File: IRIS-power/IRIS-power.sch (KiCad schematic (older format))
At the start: 66 parts, among them J2 Powerpole, J3 PJ-047AH

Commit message: Added new 5V rail, adjusted passives, added fuel gauge
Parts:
- removed C11: 1nF, Capacitor_SMD:C_0603_1608Metric, symbol Device:C
- removed C12, C14, C23: 10uF, Capacitor_SMD:C_1206_3216Metric, symbol Device:C
- removed C15: 10pF, Capacitor_SMD:C_0603_1608Metric, symbol Device:C
- removed C16: 1.2nF, Capacitor_SMD:C_0603_1608Metric, symbol Device:C
- removed C17, C20: 100nF, Capacitor_SMD:C_0603_1608Metric, symbol Device:C
- removed C18: 68nF, Capacitor_SMD:C_0603_1608Metric, symbol Device:C
- removed C21, C22: 22uF, Capacitor_SMD:C_1206_3216Metric, symbol Device:C
- removed C6: 150uF, Capacitor_SMD:C_1210_3225Metric, symbol Device:C
- removed C9: 220nF, Capacitor_SMD:C_0603_1608Metric, symbol Device:C
- removed D1: FSV1045V, STARpower:TO-227, symbol Device:D_Schottky
- removed L1: 1.5uH, STARpower:744314150, symbol Device:L
- removed L2: 3.3uH, STARpower:744316330, symbol Device:L
- removed L3: 10uH, STARpower:7443251000, symbol Device:L
- removed R1: 7.5k, Resistor_SMD:R_0603_1608Metric, symbol Device:R
- removed R11: 51.1R, Resistor_SMD:R_0603_1608Metric, symbol Device:R
- removed R12: 6.04k, Resistor_SMD:R_0603_1608Metric, symbol Device:R
- removed R15: 2.26k, Resistor_SMD:R_0603_1608Metric, symbol Device:R
- removed R17: 54.9k, Resistor_SMD:R_0603_1608Metric, symbol Device:R
- removed R18: 10k, Resistor_SMD:R_0603_1608Metric, symbol Device:R
- removed R2: 2.49k, Resistor_SMD:R_0603_1608Metric, symbol Device:R
- removed R3: 3.3k, Resistor_SMD:R_0603_1608Metric, symbol Device:R
- removed R6: 3320k, Resistor_SMD:R_0603_1608Metric, symbol Device:R
- removed R7: 1910k, Resistor_SMD:R_0603_1608Metric, symbol Device:R
- removed TP5, TP7: TestPoint, TestPoint:TestPoint_Loop_D2.60mm_Drill1.6mm_Beaded, symbol Connector:TestPoint
- removed U?: TPS565201, Package_TO_SOT_SMD:TSOT-23-6, symbol star-common-lib:TPS565201
- added C? (x3): 47uF, symbol Device:C
- added C? (x2): 10uF, symbol Device:C
- added C?: 68nF, symbol Device:C
- added C?: 1.2nF, symbol Device:C
- added C?: 0.47uF, symbol Device:C
- added C? (x2): 0.1uF, symbol Device:C
- added D?: D_Schottky, Diode_SMD:D_SMA_Handsoldering, symbol Device:D_Schottky
- added F?: Polyfuse, symbol Device:Polyfuse
- added JP? (x2): Jumper_3_Bridged12, symbol Jumper:Jumper_3_Bridged12
- added L?: 8.2uH, symbol Device:L
- added L?: 1.5uH, symbol Device:L
- added NT? (x4): Net-Tie_2, symbol Device:Net-Tie_2
- added Q?: 2N7002, Package_TO_SOT_SMD:SOT-23, symbol Transistor_FET:2N7002
- added Q?: IRLML6402, Package_TO_SOT_SMD:SOT-23, symbol Transistor_FET:IRLML6402
- added R? (x4): 10k, symbol Device:R
- added R? (x2): 2.49k, symbol Device:R
- added R? (x2): 3k, symbol Device:R
- added R?: 3570k, symbol Device:R
- added R?: 1150k, symbol Device:R
- added R?: 2m, symbol Device:R_Shunt
- added R?: 301k, symbol Device:R
- added R?: 200k, symbol Device:R
- added R?: 499k, symbol Device:R
- added U?: TPSM53604, symbol star-common-lib:TPSM53604
- added U?: MAX17261, symbol star-common-lib:MAX17261
- R13: value 976k -> 1.1M
- R14: value 133k -> 150k
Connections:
- net labels added: -BATT, CAPOK, FB_HV_N, FB_HV_P, GND1, GNDS, SCL, SDA, ~CHRG, ~CMPOUT
- net labels removed: FB, FBVcap, FB_HV, SVsys, Vcap, Vmid
- wire segments 193 -> 197
- no-connect marks 25 -> 26
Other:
- note added: "Battery Fuel Gauge"
- note added: "Charge at 1A"
- note added: "Note 1"
- note added: "Note 1: Feedback resistors should have tolerance less than 1%"
- note added: "Note 2"
- note added: "Note 2: Vcap set at 4.5V, CMPIN falling threshold when 1/2 Vcap"
- note removed: "Charge current \nlimit 500mA"
- note removed: "LiPo/DC Auto-Switching Mux"
- note removed: "Low when normal"
- note removed: "Set Vcap 5V"
- note removed: "e"
- moved on the sheet: C1, C10, C13, C19, C2, C24, C25, C3, C4, C5, C7, C8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

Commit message: Added more input protection, revised schematic
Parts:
- removed C13: 100nF, Capacitor_SMD:C_0603_1608Metric, symbol Device:C
- removed C25: 680nF, Capacitor_SMD:C_0603_1608Metric, symbol Device:C
- removed C8: 1uF, Capacitor_SMD:C_0603_1608Metric, symbol Device:C
- removed F?: Polyfuse, symbol Device:Polyfuse
- removed R10: 21.5k, Resistor_SMD:R_0603_1608Metric, symbol Device:R
- removed R4: 15k, Resistor_SMD:R_0603_1608Metric, symbol Device:R
- removed R5: 16k, Resistor_SMD:R_0603_1608Metric, symbol Device:R
- removed TP1, TP2, TP3, TP4, TP6: TestPoint, TestPoint:TestPoint_Loop_D2.60mm_Drill1.6mm_Beaded, symbol Connector:TestPoint
- added C? (x2): 1uF, symbol Device:C
- added C?: 10uF, symbol Device:C
- added C?: 0.1uF, symbol Device:C
- added C?: 0.47uF, symbol Device:C
- added D?: D_Schottky, Diode_SMD:D_SMA_Handsoldering, symbol Device:D_Schottky
- added R?: 38.3k, symbol Device:R
- added R?: 2.49k, symbol Device:R
- added R?: 1k, symbol Device:R
- added U?: TLV75733PDBV, Package_TO_SOT_SMD:SOT-23-5, symbol Regulator_Linear:TLV75733PDBV
- added U? (x2): TVS1400DRV, Package_SON:WSON-6-1EP_2x2mm_P0.65mm_EP1x1.6mm, symbol Power_Protection:TVS1400DRV
- R?: renamed from R9; value 10k -> 2.49k
- renumbered C19 to C?, C10 to C?, C24 to C?, C3 to C?, C4 to C?, C1 to C?, C2 to C?, C5 to C?, C7 to C?, H1 to H?, H2 to H?, H3 to H?, H4 to H?, J2 to J?, J3 to J?, R16 to R?, R19 to R?, R8 to R?, R20 to R?, R13 to R?, R14 to R?
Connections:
- net labels added: CELLX, FB, Vcap, Vmid
- wire segments 197 -> 204
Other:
- note added: "6V - 12.6V LiPo"
- note added: "9V - 12V DC jack"
- note added: "Auto-switching Power Mux"
- note added: "Min CP2: 1.19V Max CP2: 2.51V"
- note added: "Min PRI: 2.57V Max PRI: 3.44V"
- note added: "Power Inputs"
- note added: "Supports 2S - 3S LiPo\nTransient voltage protected"
- note added: "Supports 9V-12V DC power\n2.1mm ID 5.5mm OD barrel jack\nTransient voltage protected"
- note added: "System current limit set at 2.8A"
- note removed: "Note 2"
- moved on the sheet: C?, D?, J?, JP?, L?, NT?, Q?, R?, U?

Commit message: updated library:
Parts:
- added J3: PCIE1X, symbol star-common-lib:PCIE1X
- gave numbers to parts that had none: 74
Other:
- moved on the sheet: C1, C10, C11, C12, C13, C14, C15, C16, C17, C18, C19, C2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

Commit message: Updated sheets organization
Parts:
- removed C1, C21, C8: 0.1uF, symbol Device:C
- removed C10: 1.2nF, symbol Device:C
- removed C11: 27nF, Capacitor_SMD:C_0603_1608Metric, symbol Device:C
- removed C12, C20, C3, C4, C5, C7: 10uF, Capacitor_SMD:C_1206_3216Metric, symbol Device:C
- removed C13, C2: 0.47uF, symbol Device:C
- removed C14, C15, C24: 10uF, symbol Device:C
- removed C16, C17, C22: 47uF, symbol Device:C
- removed C18, C19: 3.3F, STARpower:SCCR20B335PRB, symbol Device:CP
- removed C23, C6: 1uF, symbol Device:C
- removed C9: 68nF, symbol Device:C
- removed D1, D2: D_Schottky, Diode_SMD:D_SMA_Handsoldering, symbol Device:D_Schottky
- removed H1, H2, H3, H4: MountingHole_Pad, MountingHole:MountingHole_3.2mm_M3_Pad_Via, symbol Mechanical:MountingHole_Pad
- removed J1: Powerpole, STARpower:1336G1, symbol Connector_Generic:Conn_01x02
- removed J2: PJ-047AH, STARpower:CUI_PJ-047AH, symbol Connector:Barrel_Jack_Switch_MountingPin
- removed J3: PCIE1X, symbol star-common-lib:PCIE1X
- removed JP1, JP2: Jumper_3_Bridged12, symbol Jumper:Jumper_3_Bridged12
- removed L1: 8.2uH, symbol Device:L
- removed L2: 1.5uH, symbol Device:L
- removed NT1, NT2, NT3, NT4: Net-Tie_2, symbol Device:Net-Tie_2
- removed Q1: 2N7002, Package_TO_SOT_SMD:SOT-23, symbol Transistor_FET:2N7002
- removed Q2: IRLML6402, Package_TO_SOT_SMD:SOT-23, symbol Transistor_FET:IRLML6402
- removed R1: 499k, symbol Device:R
- removed R10: 38.3k, symbol Device:R
- removed R11, R16, R6: 2.49k, symbol Device:R
- removed R12: 38.3k, Resistor_SMD:R_0603_1608Metric, symbol Device:R
- removed R13: 232k, Resistor_SMD:R_0603_1608Metric, symbol Device:R
- removed R14, R8: 10k, Resistor_SMD:R_0603_1608Metric, symbol Device:R
- removed R15, R17, R19, R4: 10k, symbol Device:R
- removed R18, R22: 3k, symbol Device:R
- removed R2: 301k, symbol Device:R
- removed R20: 3570k, symbol Device:R
- removed R21: 1150k, symbol Device:R
- removed R23: 1.1M, Resistor_SMD:R_0603_1608Metric, symbol Device:R
- removed R24: 150k, Resistor_SMD:R_0603_1608Metric, symbol Device:R
- removed R3: 200k, symbol Device:R
- removed R5: 2m, symbol Device:R_Shunt
- removed R7: 1k, symbol Device:R
- removed R9: 2.49k, Resistor_SMD:R_0603_1608Metric, symbol Device:R
- removed U1, U2: TVS1400DRV, Package_SON:WSON-6-1EP_2x2mm_P0.65mm_EP1x1.6mm, symbol Power_Protection:TVS1400DRV
- removed U3: MAX17261, symbol star-common-lib:MAX17261
- removed U4: TPS2121, symbol star-common-lib:TPS2121
- removed U5: TPS55340, symbol star-common-lib:TPS55340
- removed U6: TPSM53604, symbol star-common-lib:TPSM53604
- removed U7: LTC3110, symbol star-common-lib:LTC3110
- removed U8: TLV75733PDBV, Package_TO_SOT_SMD:SOT-23-5, symbol Regulator_Linear:TLV75733PDBV
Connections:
- net labels removed: +29.5V, +3.3V, +5V, +BATT, +MUX, -BATT, CAPOK, CAP_STAT, CELLX, COMP, DIR, FB, FB_HV_N, FB_HV_P, FREQ, GND, GND1, GNDS, PROG, PWR_STAT, SCL, SDA, SS, VDC, VDD, Vcap, Vmid, ~CHRG, ~CMPOUT
- wire segments 204 -> 37
- no-connect marks 26 -> 0
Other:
- note removed: "+29.5V SiPM Supply"
- note removed: "5V Backup"
- note removed: "5V Regulator"
- note removed: "6V - 12.6V LiPo"
- note removed: "9V - 12V DC jack"
- note removed: "Auto-switching Power Mux"
- note removed: "Battery Fuel Gauge"
- note removed: "Charge at 1A"
- note removed: "Min CP2: 1.19V Max CP2: 2.51V"
- note removed: "Min PRI: 2.57V Max PRI: 3.44V"
- note removed: "Note 1"
- note removed: "Output\nset 5V"
- note removed: "Power Inputs"
- note removed: "Supports 2S - 3S LiPo\nTransient voltage protected"
- note removed: "Supports 9V-12V DC power\n2.1mm ID 5.5mm OD barrel jack\nTransient voltage protected"
- note removed: "System current limit set at 2.8A"

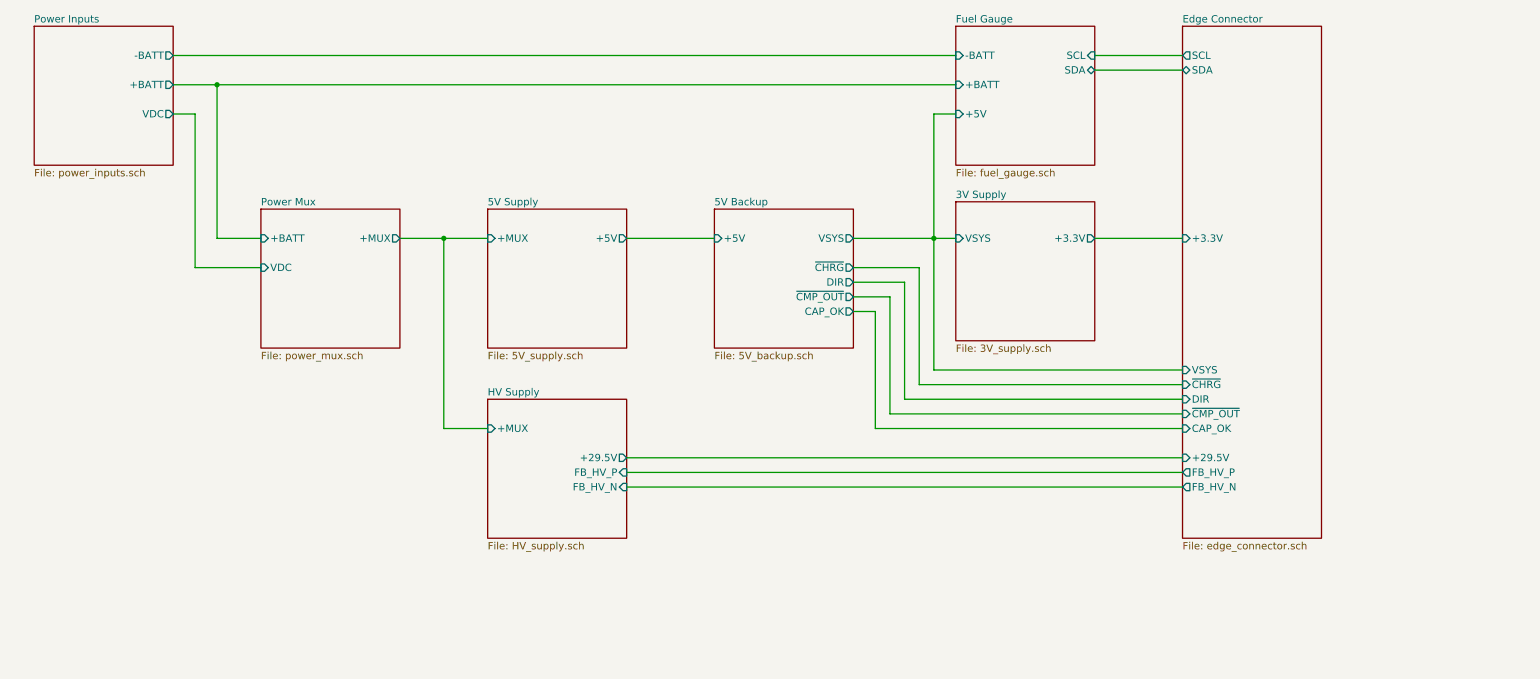
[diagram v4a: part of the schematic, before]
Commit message: Finalized power board V2 schematic, preparing to layout
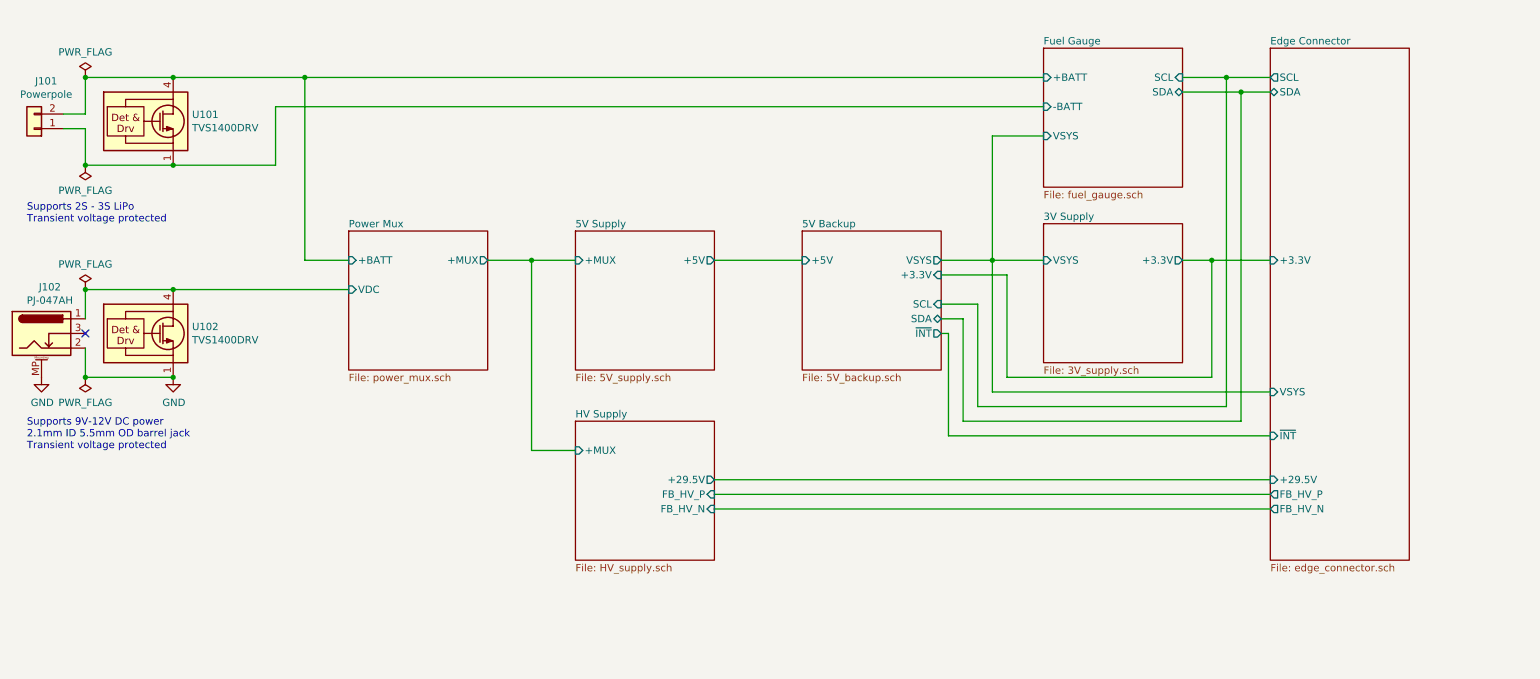
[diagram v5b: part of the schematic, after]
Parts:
- added J101: Powerpole, star-common-lib:Powerpole_1336G1, symbol Connector_Generic:Conn_01x02
- added J102: PJ-047AH, star-common-lib:CUI_PJ-047AH, symbol Connector:Barrel_Jack_Switch_MountingPin
- added U101, U102: TVS1400DRV, Package_SON:WSON-6-1EP_2x2mm_P0.65mm_EP1x1.6mm, symbol star-common-lib:TVS1400DRV
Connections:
- net Fuel Gauge/+BATT: now also J101.2 (Pin_2), U101.4 (IN), U101.5 (IN), U101.6 (IN)
- net Fuel Gauge/-BATT: now also J101.1 (Pin_1), U101.1 (GND), U101.2 (GND), U101.3 (GND), U101.7 (GND)
- new net GND: J102.2, J102.MP (MountPin), U102.1 (GND), U102.2 (GND), U102.3 (GND), U102.7 (GND)
- new net Power Mux/VDC: J102.1, U102.4 (IN), U102.5 (IN), U102.6 (IN)
- no-connect marks 0 -> 1
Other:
- note added: "Supports 2S - 3S LiPo\nTransient voltage protected"
- note added: "Supports 9V-12V DC power\n2.1mm ID 5.5mm OD barrel jack\nTransient voltage protected"

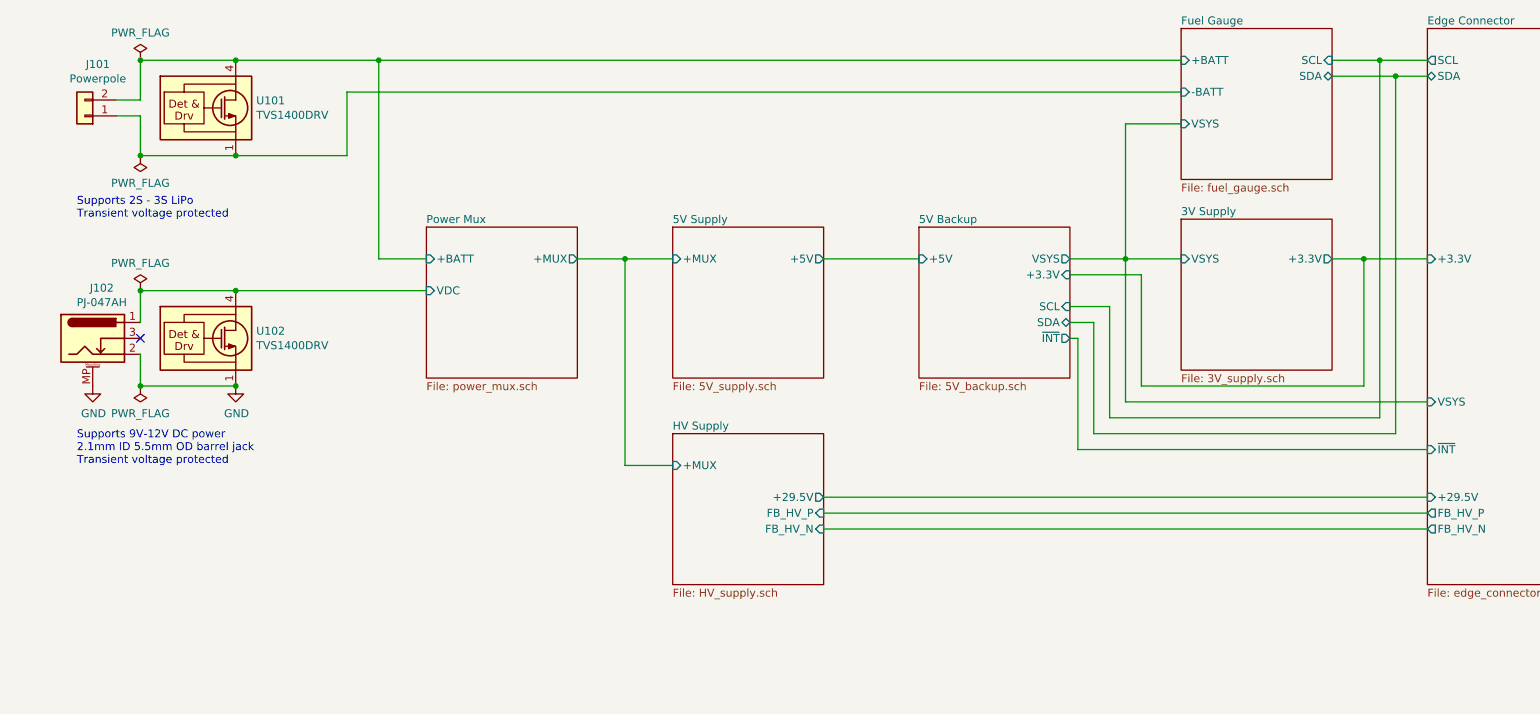
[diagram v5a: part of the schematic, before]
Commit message: Updated layout
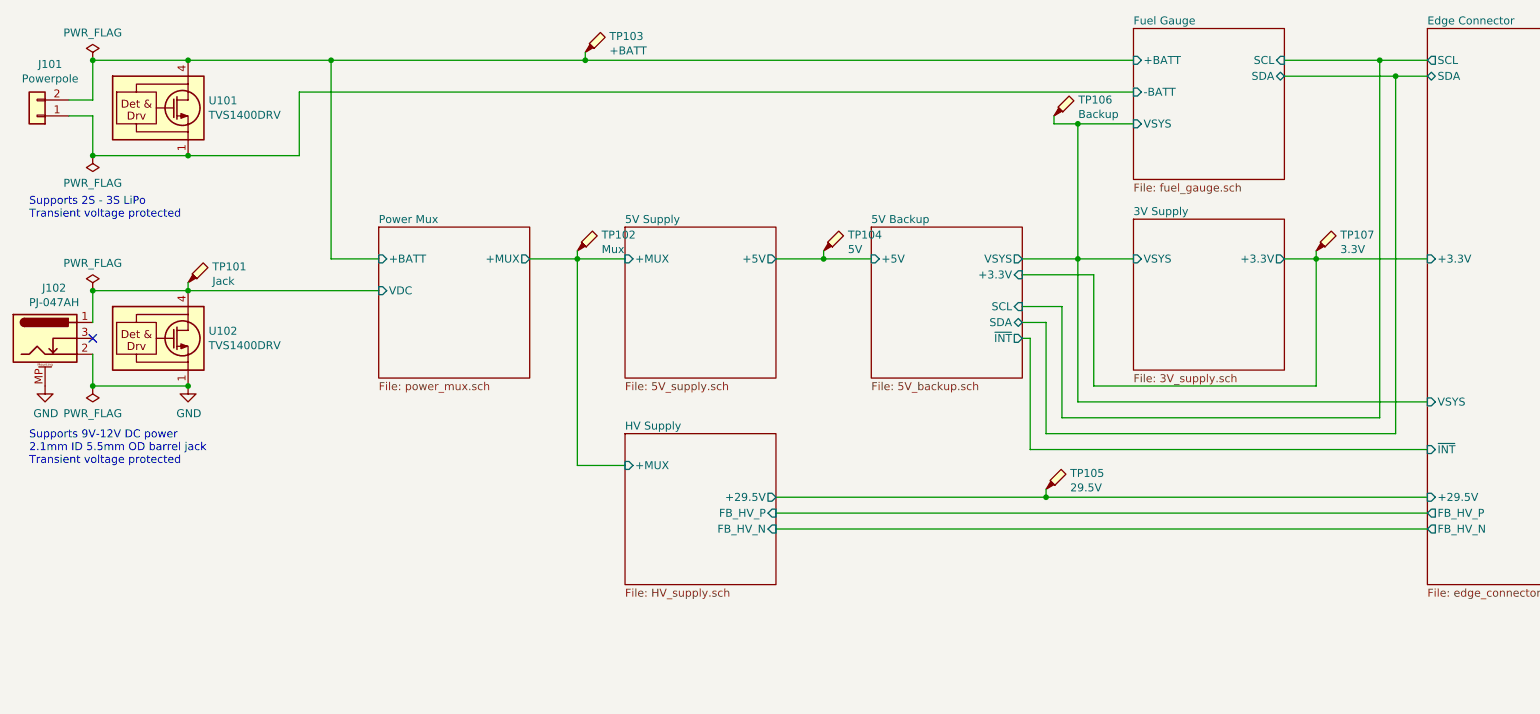
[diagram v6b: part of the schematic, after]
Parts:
- added TP101: Jack, TestPoint:TestPoint_Keystone_5000-5004_Miniature, symbol Connector:TestPoint_Probe
- added TP102: Mux, TestPoint:TestPoint_Keystone_5000-5004_Miniature, symbol Connector:TestPoint_Probe
- added TP103: +BATT, TestPoint:TestPoint_Keystone_5000-5004_Miniature, symbol Connector:TestPoint_Probe
- added TP104: 5V, TestPoint:TestPoint_Keystone_5000-5004_Miniature, symbol Connector:TestPoint_Probe
- added TP105: 29.5V, TestPoint:TestPoint_Keystone_5000-5004_Miniature, symbol Connector:TestPoint_Probe
- added TP106: Backup, TestPoint:TestPoint_Keystone_5000-5004_Miniature, symbol Connector:TestPoint_Probe
- added TP107: 3.3V, TestPoint:TestPoint_Keystone_5000-5004_Miniature, symbol Connector:TestPoint_Probe
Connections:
- net 3V Supply/+3.3V: now also TP107.1
- net 3V Supply/VSYS: now also TP106.1
- net 5V Backup/+5V: now also TP104.1
- net 5V Supply/+MUX: now also TP102.1
- net Edge Connector/+29.5V: now also TP105.1
- net Fuel Gauge/+BATT: now also TP103.1
- net Power Mux/VDC: now also TP101.1
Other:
- moved on the sheet: J101, J102, U101, U102
